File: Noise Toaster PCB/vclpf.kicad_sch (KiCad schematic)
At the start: 20 parts, among them Q5 2N5457, U2 LM324, X12 Conn_01x01_Pin

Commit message: applied footprints
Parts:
- C10, C12, C8, C9: footprint (none) -> Capacitor_THT:C_Disc_D5.1mm_W3.2mm_P5.00mm
- Q5: footprint (none) -> Package_TO_SOT_THT:TO-92_Inline
- R27, R33, R34, R35, R36, R39, R40, R44, R45: footprint (none) -> Resistor_THT:R_Axial_DIN0207_L6.3mm_D2.5mm_P10.16mm_Horizontal
- U2: footprint (none) -> Package_DIP:DIP-14_W7.62mm_Socket
- X12: footprint (none) -> Connector_PinHeader_1.00mm:PinHeader_1x01_P1.00mm_Vertical
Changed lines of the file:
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@@
       (effects (font (size 1.27 1.27)) (justify right))
     )
-    (property "Footprint" "" (at 148.59 53.848 90)
+    (property "Footprint" "Resistor_THT:R_Axial_DIN0207_L6.3mm_D2.5mm_P10.16mm_Horizontal" (at 148.59 53.848 90)
       (effects (font (size 1.27 1.27)) hide)
     )
@@
       (effects (font (size 1.27 1.27)) (justify right))
     )
-    (property "Footprint" "" (at 222.25 116.078 90)
+    (property "Footprint" "Resistor_THT:R_Axial_DIN0207_L6.3mm_D2.5mm_P10.16mm_Horizontal" (at 222.25 116.078 90)
       (effects (font (size 1.27 1.27)) hide)
     )
@@
       (effects (font (size 1.27 1.27)))
     )
-    (property "Footprint" "" (at 41.91 140.97 0)
+    (property "Footprint" "Package_DIP:DIP-14_W7.62mm_Socket" (at 41.91 140.97 0)
       (effects (font (size 1.27 1.27)) hide)
     )
@@
       (effects (font (size 1.27 1.27)) (justify right))
     )
-    (property "Footprint" "" (at 222.25 93.218 90)
+    (property "Footprint" "Resistor_THT:R_Axial_DIN0207_L6.3mm_D2.5mm_P10.16mm_Horizontal" (at 222.25 93.218 90)
       (effects (font (size 1.27 1.27)) hide)
     )
@@
       (effects (font (size 1.27 1.27)))
     )
-    (property "Footprint" "" (at 180.34 155.448 90)
+    (property "Footprint" "Resistor_THT:R_Axial_DIN0207_L6.3mm_D2.5mm_P10.16mm_Horizontal" (at 180.34 155.448 90)
       (effects (font (size 1.27 1.27)) hide)
     )
@@
       (effects (font (size 1.27 1.27)))
     )
-    (property "Footprint" "" (at 184.15 113.3348 0)
+    (property "Footprint" "Capacitor_THT:C_Disc_D5.1mm_W3.2mm_P5.00mm" (at 184.15 113.3348 0)
       (effects (font (size 1.27 1.27)) hide)
     )
@@
       (effects (font (size 1.27 1.27)) (justify left) hide)
     )
-    (property "Footprint" "" (at 101.6 50.8 0)
+    (property "Footprint" "Connector_PinHeader_1.00mm:PinHeader_1x01_P1.00mm_Vertical" (at 101.6 50.8 0)
       (effects (font (size 1.27 1.27)) hide)
     )
@@
       (effects (font (size 1.27 1.27)) (justify left))
     )
-    (property "Footprint" "" (at 256.54 88.9 0)
+    (property "Footprint" "Package_TO_SOT_THT:TO-92_Inline" (at 256.54 88.9 0)
       (effects (font (size 1.27 1.27)) hide)
     )
@@
       (effects (font (size 1.27 1.27)) (justify right))
     )
-    (property "Footprint" "" (at 58.928 110.49 90)
+    (property "Footprint" "Resistor_THT:R_Axial_DIN0207_L6.3mm_D2.5mm_P10.16mm_Horizontal" (at 58.928 110.49 90)
       (effects (font (size 1.27 1.27)) hide)
     )
@@
       (effects (font (size 1.27 1.27)))
     )
-    (property "Footprint" "" (at 139.7 37.1348 0)
+    (property "Footprint" "Capacitor_THT:C_Disc_D5.1mm_W3.2mm_P5.00mm" (at 139.7 37.1348 0)
       (effects (font (size 1.27 1.27)) hide)
     )
@@
       (effects (font (size 1.27 1.27)) (justify left) hide)
     )
-    (property "Footprint" "" (at 49.53 140.97 0)
+    (property "Footprint" "Package_DIP:DIP-14_W7.62mm_Socket" (at 49.53 140.97 0)
       (effects (font (size 1.27 1.27)) hide)
     )
@@
       (effects (font (size 1.27 1.27)) (justify left) hide)
     )
-    (property "Footprint" "" (at 153.67 114.3 0)
+    (property "Footprint" "Connector_PinHeader_1.00mm:PinHeader_1x01_P1.00mm_Vertical" (at 153.67 114.3 0)
       (effects (font (size 1.27 1.27)) hide)
     )
@@
       (effects (font (size 1.27 1.27)))
     )
-    (property "Footprint" "" (at 53.34 74.168 90)
+    (property "Footprint" "Resistor_THT:R_Axial_DIN0207_L6.3mm_D2.5mm_P10.16mm_Horizontal" (at 53.34 74.168 90)
       (effects (font (size 1.27 1.27)) hide)
     )
@@
       (effects (font (size 1.27 1.27)) (justify left))
     )
-    (property "Footprint" "" (at 234.442 58.42 90)
+    (property "Footprint" "Resistor_THT:R_Axial_DIN0207_L6.3mm_D2.5mm_P10.16mm_Horizontal" (at 234.442 58.42 90)
       (effects (font (size 1.27 1.27)) hide)
     )
@@
       (effects (font (size 1.27 1.27)) (justify left) hide)
     )
-    (property "Footprint" "" (at 30.48 30.48 0)
+    (property "Footprint" "Connector_PinHeader_1.00mm:PinHeader_1x01_P1.00mm_Vertical" (at 30.48 30.48 0)
       (effects (font (size 1.27 1.27)) hide)
     )
@@
       (effects (font (size 1.27 1.27)))
     )
-    (property "Footprint" "" (at 97.79 127.9652 0)
+    (property "Footprint" "Capacitor_THT:C_Disc_D5.1mm_W3.2mm_P5.00mm" (at 97.79 127.9652 0)
       (effects (font (size 1.27 1.27)) hide)
     )
@@
       (effects (font (size 1.27 1.27)))
     )
-    (property "Footprint" "" (at 168.91 39.878 90)
+    (property "Footprint" "Resistor_THT:R_Axial_DIN0207_L6.3mm_D2.5mm_P10.16mm_Horizontal" (at 168.91 39.878 90)
       (effects (font (size 1.27 1.27)) hide)
     )
@@
       (effects (font (size 1.27 1.27)) (justify left) hide)
     )
-    (property "Footprint" "" (at 123.19 114.3 0)
+    (property "Footprint" "Connector_PinHeader_1.00mm:PinHeader_1x01_P1.00mm_Vertical" (at 123.19 114.3 0)
       (effects (font (size 1.27 1.27)) hide)
     )
@@
       (effects (font (size 1.27 1.27)) (justify left) hide)
     )
-    (property "Footprint" "" (at 105.41 170.18 0)
+    (property "Footprint" "Connector_PinHeader_1.00mm:PinHeader_1x01_P1.00mm_Vertical" (at 105.41 170.18 0)
       (effects (font (size 1.27 1.27)) hide)
     )
@@
       (effects (font (size 1.27 1.27)))
     )
-    (property "Footprint" "" (at 121.92 71.4248 0)
+    (property "Footprint" "Capacitor_THT:C_Disc_D5.1mm_W3.2mm_P5.00mm" (at 121.92 71.4248 0)
       (effects (font (size 1.27 1.27)) hide)
     )
@@
       (effects (font (size 1.27 1.27)) (justify right))
     )
-    (property "Footprint" "" (at 162.56 74.168 90)
-      (effects (font (size 1.27 1.27)) hide)
-    )
+    (property "Footprint" "Resistor_THT:R_Axial_DIN0207_L6.3mm_D2.5mm_P10.16mm_Horizontal" (at 162.56 74.168 90)
+      (effects (font (size 1.27 1.27)) hide)
+    )

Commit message: placed pards of the pcb properly
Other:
- company: http://musicfromouterspace.com/analogsynth_new/NOISETOASTER/NOISETOASTER.php -> Music From Outer Space LLC
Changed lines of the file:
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@@
     (title "Voltage Controlled Low Pass Filter")
     (rev "0.5")
-    (company "http://musicfromouterspace.com/analogsynth_new/NOISETOASTER/NOISETOASTER.php")
+    (company "Music From Outer Space LLC")
     (comment 1 "Licence: CC-BY-NC-SA")
     (comment 2 "Original Design by Ray Wilson")
-    (comment 3 "Music From Outer Space LLC")
+    (comment 3 "http://musicfromouterspace.com/analogsynth_new/NOISETOASTER/NOISETOASTER.php")
   )
   (junction (at 185.42 72.39) (diameter 0) (color 0 0 0 0)

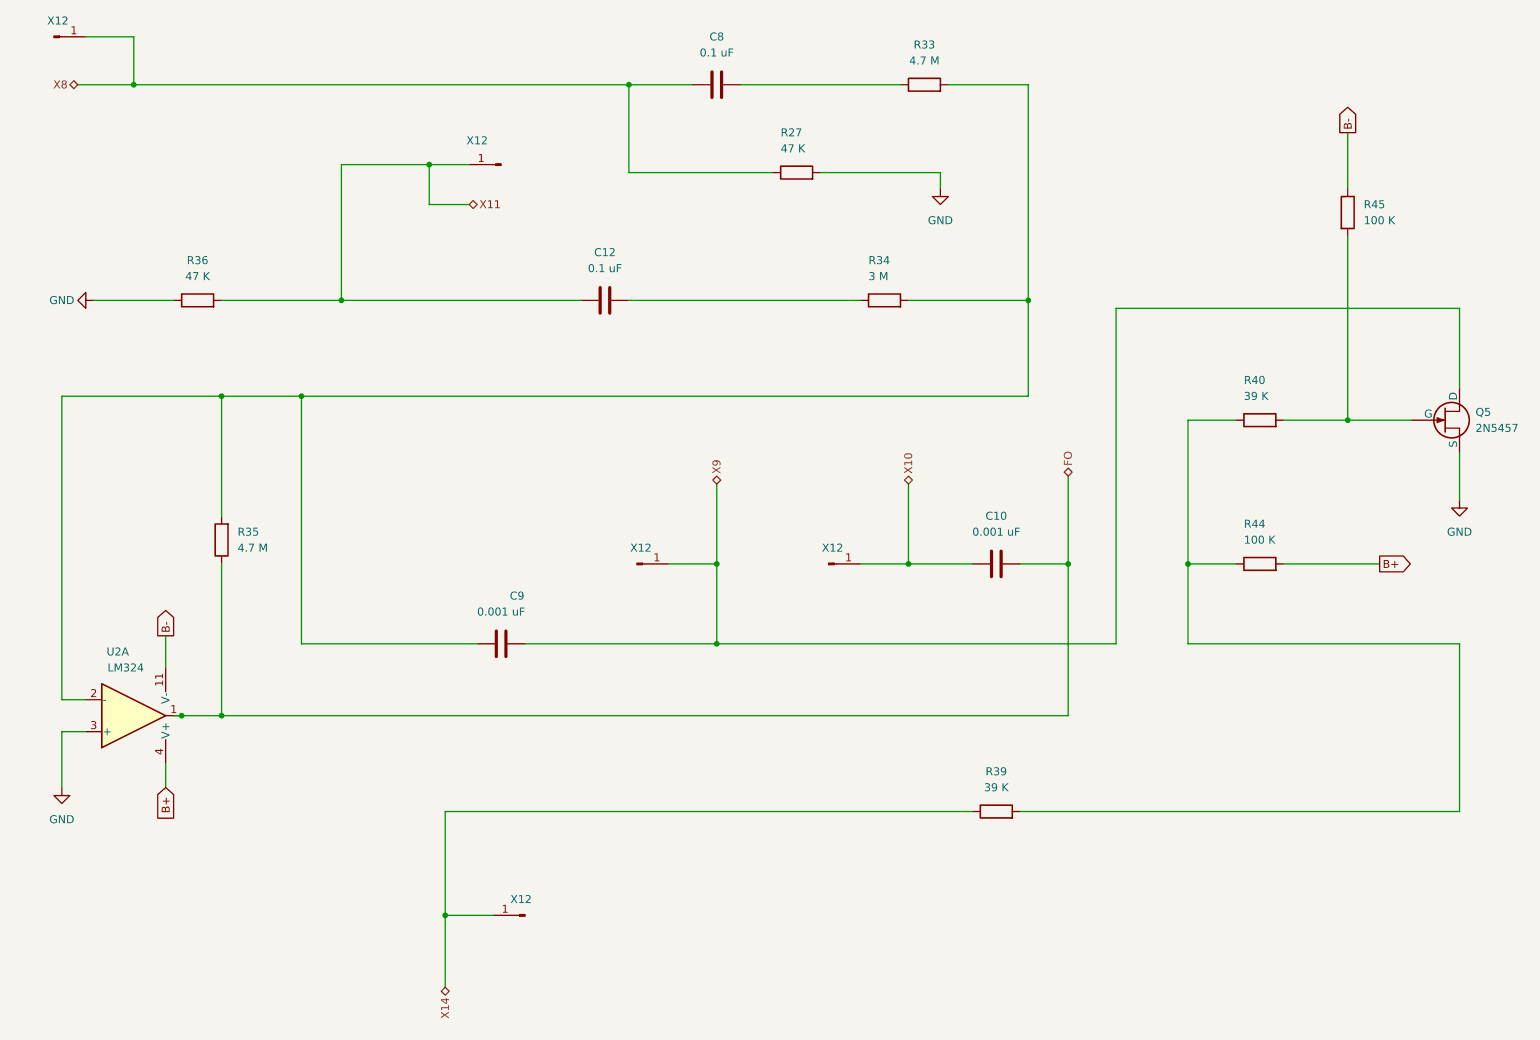
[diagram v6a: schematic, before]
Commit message: changed header pins to groups
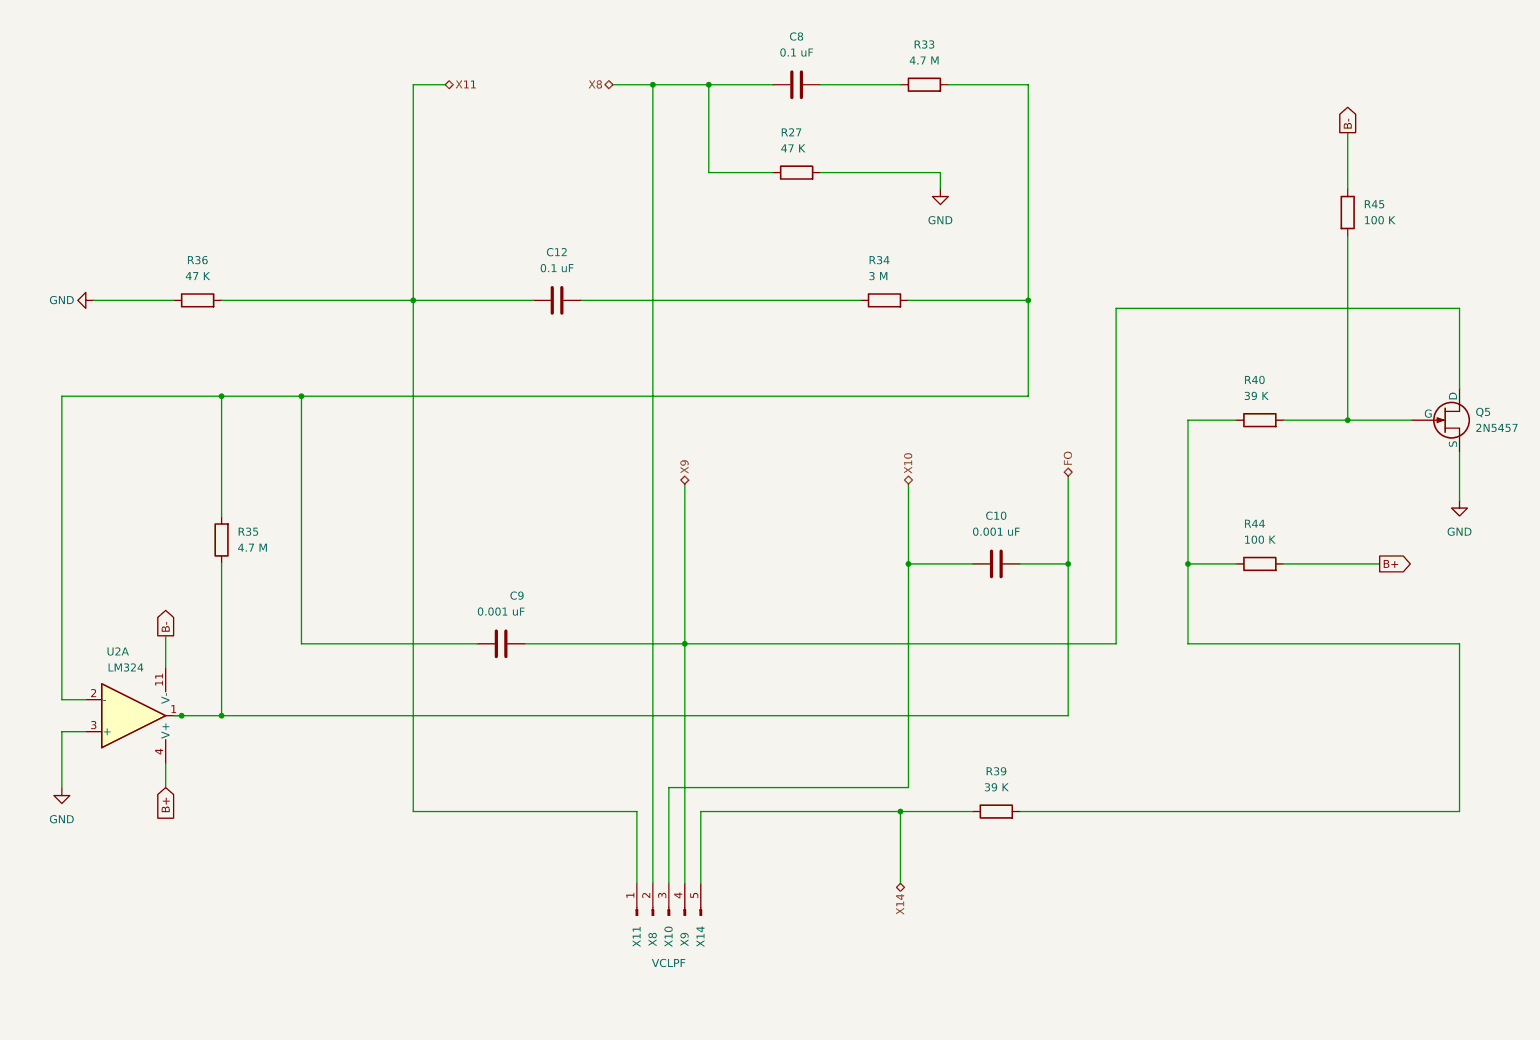
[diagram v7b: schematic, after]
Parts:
- removed X12 (x5): Conn_01x01_Pin, Connector_PinHeader_1.00mm:PinHeader_1x01_P1.00mm_Vertical, symbol Connector:Conn_01x01_Pin
- added J7: VCLPF, Connector_PinHeader_2.00mm:PinHeader_1x05_P2.00mm_Vertical, symbol Connector:Conn_01x05_Pin
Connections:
- net X10: now also J7.3 (Pin_3)
- net X11: now also J7.1 (Pin_1)
- net X14: now also J7.5 (Pin_5)
- net X8: now also J7.2 (Pin_2)
- net X9: now also J7.4 (Pin_4)
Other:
- moved on the sheet: C12, C8
